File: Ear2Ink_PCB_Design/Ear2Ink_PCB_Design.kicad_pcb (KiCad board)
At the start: 2 copper layers, 68 parts, among them J1 Conn_02x16_Top_Bottom, J2 Conn_01x08_Pin, J3 Conn_01x08_Pin, J4 MEM2052-00-195-00-A_REVA, J5 Conn_01x06_Pin, J6 Conn_01x04_Pin, J7 Conn_01x03_Pin, P1 OSTTE020104, SW1 SW_Push, U1 STM32F411RETx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

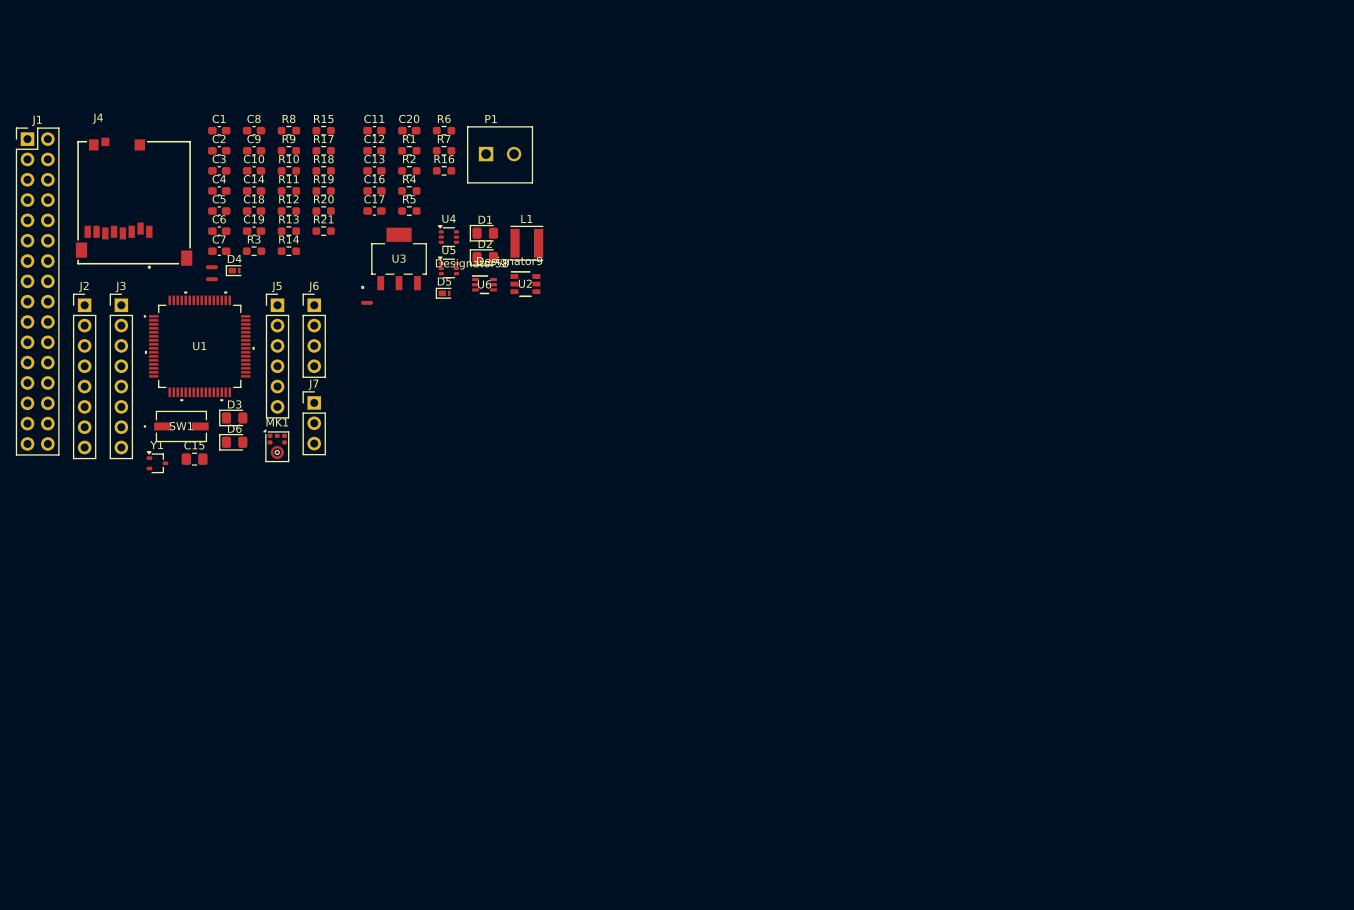
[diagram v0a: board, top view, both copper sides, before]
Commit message: components on board (no traces yet)
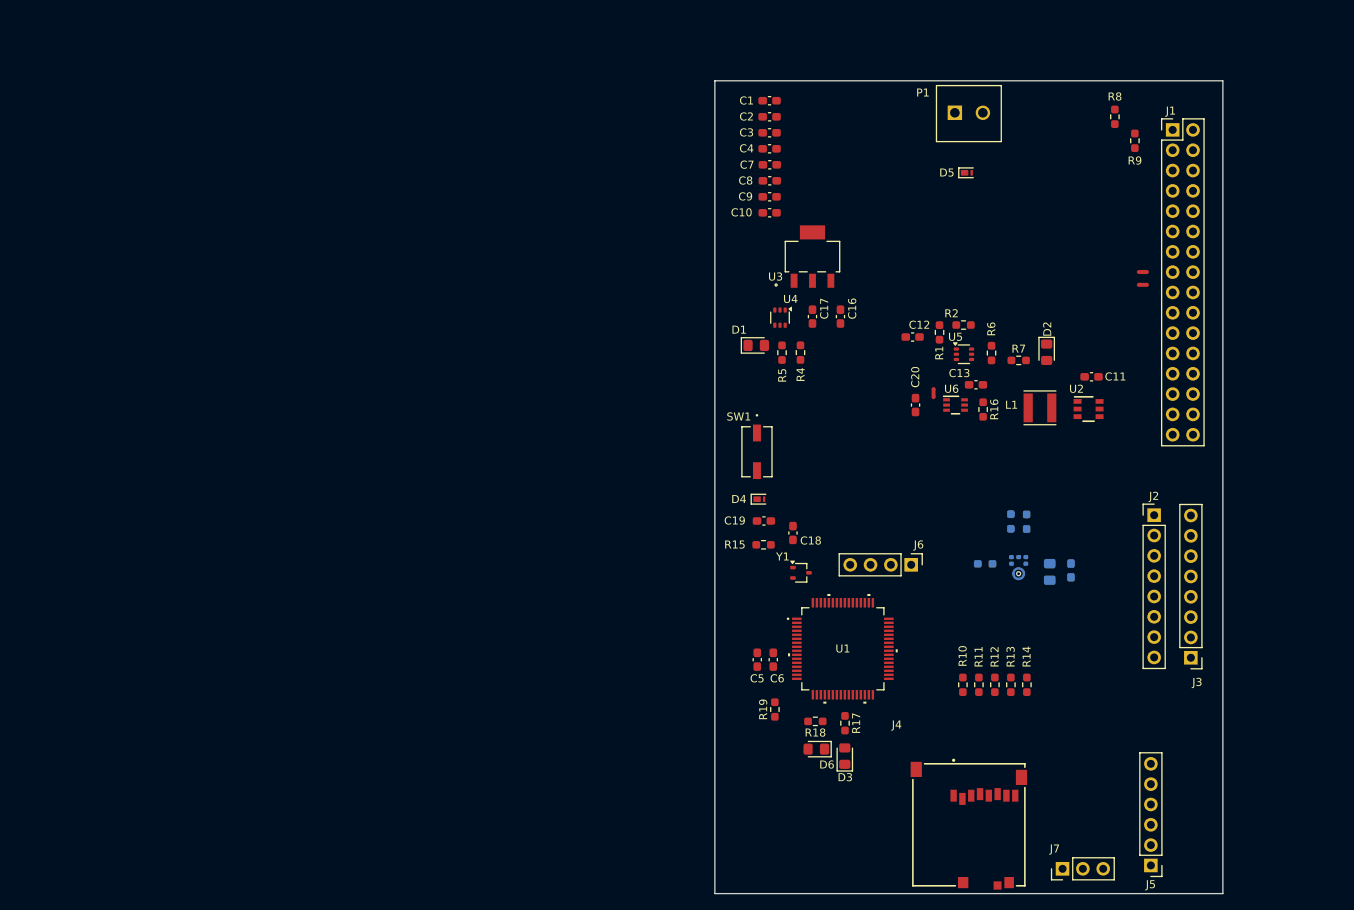
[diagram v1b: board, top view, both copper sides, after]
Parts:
- C14, C15, MK1, R20, R21, R3: moved to B.Cu
- moved J1 143.1 mm to (188.2, 37.1)
- moved J3 140.8 mm to (190.5, 103.1), turned to 180 degrees
- moved J2 136.2 mm to (185.9, 85.3)
- moved J4 130.1 mm to (162.8, 124.0), turned to 180 degrees
- moved J5 129.7 mm to (185.5, 129.1), turned to 180 degrees
- moved NT3 116.4 mm to (184.5, 56.5), turned to 180 degrees
- moved NT2 116.4 mm to (184.5, 54.9), turned to 180 degrees
- moved C14 112.6 mm to (175.5, 92.2), turned to -90 degrees
- moved J7 110.2 mm to (174.5, 129.5), turned to 90 degrees
- moved C15 107.8 mm to (172.9, 92.4), turned to -90 degrees
- moved R14 107.0 mm to (170.0, 106.5), turned to 90 degrees
- moved R13 106.6 mm to (168.0, 106.5), turned to 90 degrees
- moved R12 106.3 mm to (166.0, 106.5), turned to 90 degrees
- moved R11 106.1 mm to (164.0, 106.5), turned to 90 degrees
- moved R10 105.9 mm to (162.0, 106.5), turned to 90 degrees
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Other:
- board outline added: 63.5 x 101.6 mm

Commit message: some routing
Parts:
- moved J7 51.3 mm to (134.0, 98.0), turned to 180 degrees
- moved R14 10.0 mm to (160.0, 106.5), turned to -90 degrees
- moved Y1 5.04 mm to (145.0, 88.7)
- moved J6 3.88 mm to (158.0, 88.5)
- moved R12 2.19 mm to (168.0, 105.6), turned to 0 degrees
- moved D2 2.07 mm to (171.0, 63.5)
- moved D1 1.81 mm to (136.0, 65.9)
- moved R18 1.39 mm to (143.6, 112.5)
- moved R13 1.10 mm to (168.0, 107.6), turned to 0 degrees
- moved C19 1.00 mm to (137.1, 85.0)
- moved D4 1.00 mm to (136.6, 82.3)
- moved SW1 1.00 mm to (136.3, 76.4)
- moved R15 0.99 mm to (137.2, 88.0)
- moved C16 0.80 mm to (147.5, 60.5)
- moved R7 0.59 mm to (168.7, 65.4), turned to 90 degrees
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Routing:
- net +3.3V: track 0.00 -> 77.6 mm
- net SPI3_MISO: track 0.00 -> 31.7 mm
- net SPI3_MOSI: track 0.00 -> 31.7 mm
- net 5V: track 0.00 -> 24.2 mm
- net SPI3_SCK: track 0.00 -> 18.7 mm
- net SD_DAT1: track 0.00 -> 17.4 mm
- net SD_DAT2: track 0.00 -> 13.4 mm
- net CS: track 0.00 -> 13.3 mm
- net +3.3VA: track 0.00 -> 9.38 mm
- net NRST: track 0.00 -> 9.30 mm
- net 9V: track 0.00 -> 8.00 mm
- net Net-(U3-VO): track 0.00 -> 7.52 mm
- net Net-(U4-ST): track 0.00 -> 6.40 mm
- net Net-(U1-PC4): track 0.00 -> 5.88 mm
- net Net-(U5-VIN): track 0.00 -> 5.67 mm
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
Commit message: some pcb
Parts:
- removed C10: 4.7uF, Capacitor_SMD:C_0603_1608Metric_Pad1.08x0.95mm_HandSolder
- removed C7, C8: 0.1uF, Capacitor_SMD:C_0603_1608Metric_Pad1.08x0.95mm_HandSolder
- added C21: 4.7uF, Capacitor_SMD:C_0603_1608Metric_Pad1.08x0.95mm_HandSolder, F.Cu at (150.0, 74.0)
- moved R17 56.9 mm to (100.5, 79.4)
- moved D3 56.9 mm to (100.5, 83.5)
- moved D6 56.9 mm to (97.0, 82.5)
- moved R18 56.9 mm to (96.9, 80.0)
- moved R19 56.3 mm to (92.0, 77.6)
- moved C5 56.3 mm to (90.0, 71.4)
- moved C6 56.3 mm to (92.0, 71.4)
- moved J7 49.0 mm to (155.5, 54.0), turned to 90 degrees
- moved C20 41.9 mm to (176.4, 34.9)
- moved U6 41.9 mm to (181.4, 34.9)
- moved NT1 41.6 mm to (178.6, 33.7)
- moved C2 41.0 mm to (152.0, 74.0), turned to -90 degrees
- moved C1 40.2 mm to (145.2, 73.0), turned to -90 degrees
- moved R16 39.2 mm to (183.4, 37.8), turned to 180 degrees
- moved U1 38.8 mm to (148.0, 63.2)
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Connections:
- U1 pad 30: unconnected-(U1-VCAP1-Pad30) -> Net-(U1-VCAP1)
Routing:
- net SD_Detect: track 0.00 -> 54.9 mm
- net R4: track 4.62 -> 56.2 mm
- net R3: track 4.62 -> 55.6 mm
- net R2: track 4.62 -> 54.3 mm
- net R1: track 4.62 -> 53.2 mm
- net +3.3V: track 77.6 -> 32.2 mm
- net I2S2_WS: track 0.00 -> 36.6 mm, vias 0 -> 1
- net C1: track 4.62 -> 40.0 mm, vias 0 -> 1
- net SYS_SWCLK: track 0.00 -> 27.0 mm
- net Net-(U2-EN): track 0.00 -> 24.9 mm
- net Net-(U5-VIN): track 5.67 -> 29.8 mm
- net SPI3_MOSI: track 31.7 -> 8.46 mm
- net SPI3_MISO: track 31.7 -> 10.4 mm
- net NRST: track 9.30 -> 27.8 mm
- net 5V: track 24.2 -> 6.31 mm
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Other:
- board size 63.5 x 101.6 mm -> 63.5 x 69.8 mm

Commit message: more progress
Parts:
- removed R10, R11, R12, R13, R14: 10k, Resistor_SMD:R_0603_1608Metric_Pad0.98x0.95mm_HandSolder
- moved D6 55.6 mm to (152.0, 90.3)
- moved R18 55.6 mm to (151.9, 87.7)
- moved D3 49.0 mm to (149.0, 76.5)
- moved R17 48.9 mm to (149.0, 72.5)
- moved R19 48.2 mm to (139.5, 69.5), turned to 180 degrees
- moved C5 46.7 mm to (136.5, 67.6), turned to -90 degrees
- moved C6 42.7 mm to (134.5, 67.6), turned to -90 degrees
- moved NT2 7.90 mm to (185.8, 63.4)
- moved J7 7.08 mm to (162.4, 55.5)
- moved C18 3.21 mm to (137.8, 56.3), turned to 0 degrees
- moved C2 2.00 mm to (154.0, 74.0)
- moved C21 2.00 mm to (152.0, 74.0)
- moved R15 1.92 mm to (140.0, 72.6)
- moved C1 1.40 mm to (144.2, 74.0)
- moved C19 1.15 mm to (140.0, 77.0)
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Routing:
- net RS: track 0.00 -> 129.1 mm, vias 0 -> 3
- net R/W: track 0.00 -> 94.1 mm, vias 0 -> 4
- net ADC10: track 0.00 -> 92.6 mm, vias 0 -> 2
- net DB4: track 0.00 -> 80.6 mm, vias 0 -> 1
- net EN: track 0.00 -> 80.5 mm, vias 0 -> 2
- net DB6: track 0.00 -> 77.6 mm, vias 0 -> 2
- net DB5: track 0.00 -> 76.2 mm, vias 0 -> 1
- net SD_Detect: track 54.9 -> 0.00 mm
- net CS: track 0.00 -> 54.2 mm
- net SPI3_MISO: track 10.4 -> 61.5 mm
- net SPI3_SCK: track 12.6 -> 57.8 mm
- net SPI3_MOSI: track 8.46 -> 49.7 mm, vias 0 -> 1
- net +3.3V: track 32.2 -> 62.5 mm
- net SD_DAT2: track 0.08 -> 28.3 mm, vias 0 -> 1
- net 9V: track 8.68 -> 35.7 mm
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- added copper zone on F.Cu, net +3.3V
- added copper zone on B.Cu, net GND
- added copper zone on F.Cu, net GND

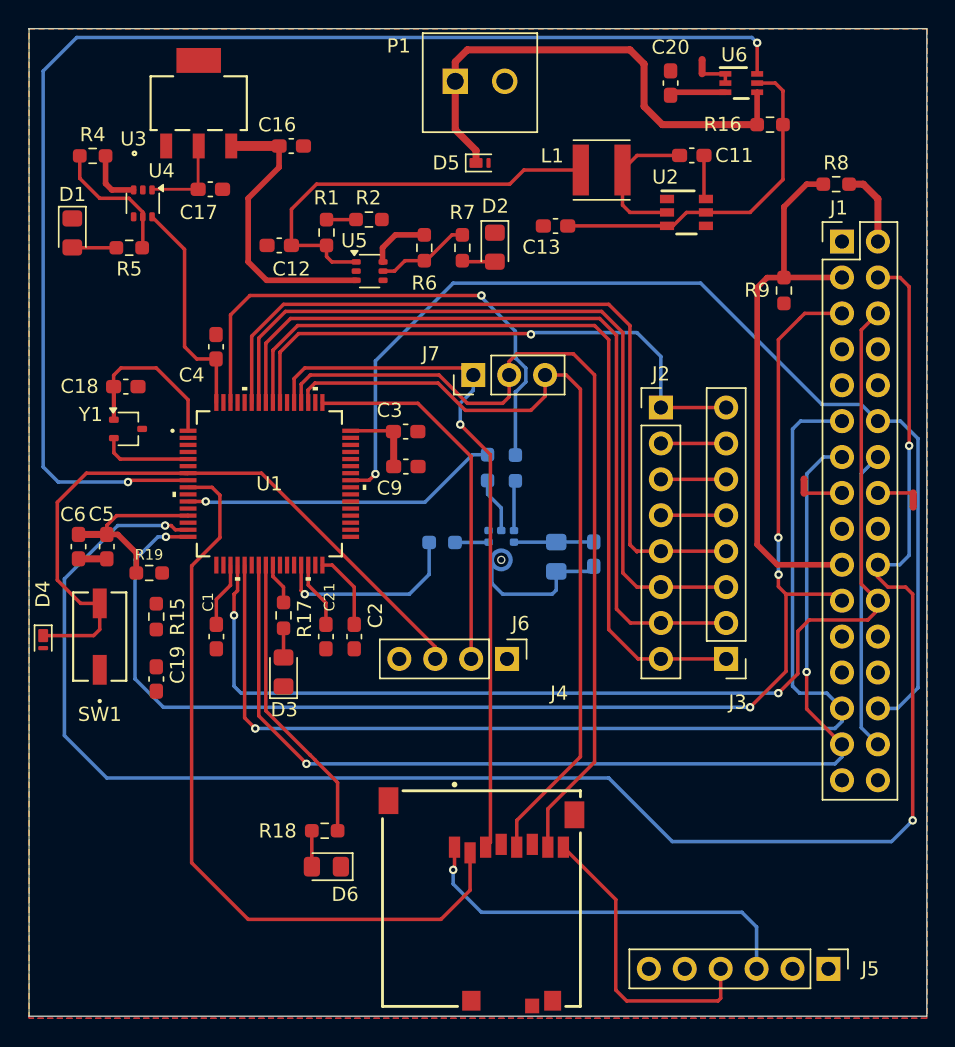
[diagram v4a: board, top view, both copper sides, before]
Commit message: ran DRC and fixed some errors
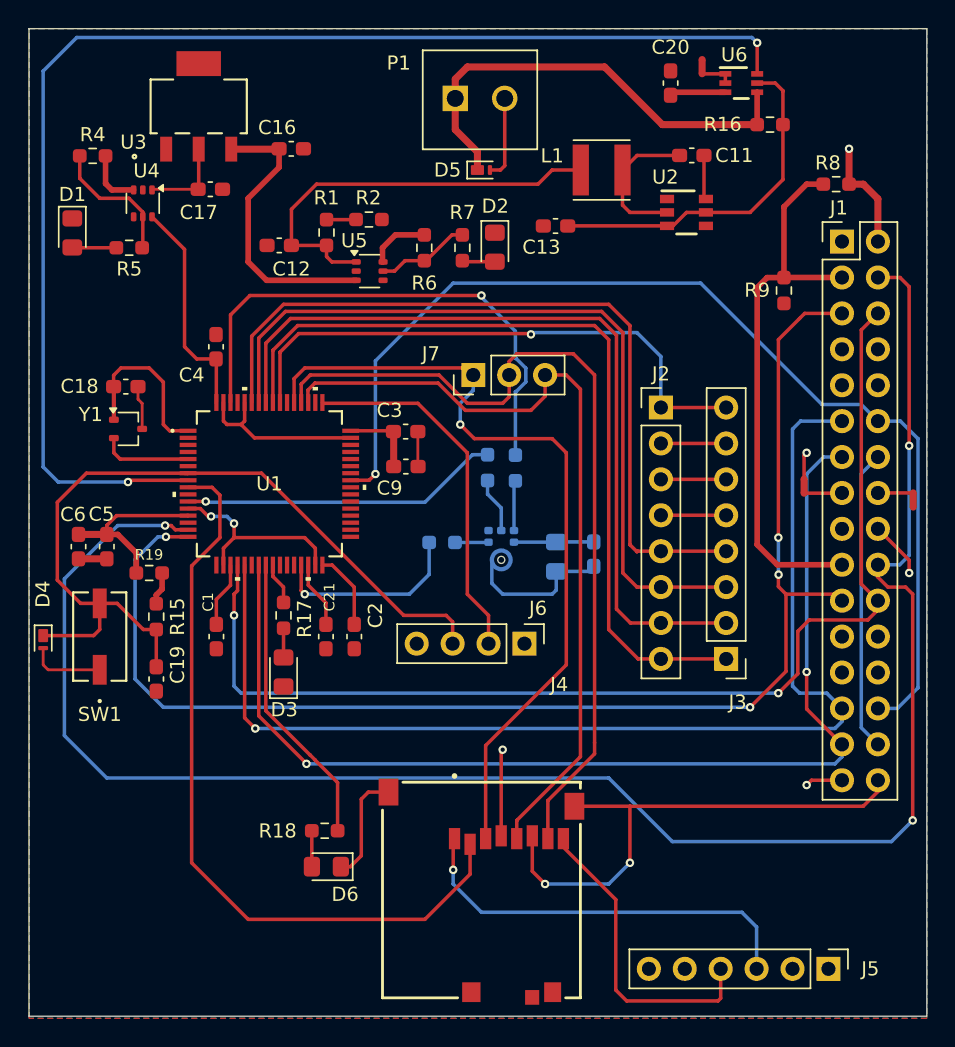
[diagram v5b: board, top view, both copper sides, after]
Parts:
- moved J6 1.64 mm to (166.0, 74.5)
- moved P1 1.21 mm to (162.9, 35.9)
- moved J4 0.61 mm to (163.0, 91.9)
- moved D5 0.51 mm to (163.0, 41.0)
- moved U3 0.23 mm to (143.0, 36.5)
- moved C16 0.20 mm to (149.5, 39.5)
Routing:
- net GND: track 12.8 -> 101.3 mm, vias 0 -> 4
- net +3.3V: track 62.5 -> 82.5 mm, vias 0 -> 5
- net NRST: track 49.1 -> 57.7 mm
- net SPI3_MOSI: track 49.7 -> 56.7 mm
- net 9V: track 35.7 -> 32.8 mm
- net SD_DAT2: track 28.3 -> 29.1 mm
- net SPI3_SCK: track 57.8 -> 57.2 mm
- net SPI3_MISO: track 61.5 -> 60.9 mm
- net SYS_SWCLK: track 26.4 -> 25.8 mm
- added copper zone on B.Cu, net +3.3V
- removed copper zone on F.Cu, net +3.3V
- removed copper zone on B.Cu, net GND

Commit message: fixed everything
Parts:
- added J8: Conn_01x16_Pin, Connector_PinHeader_2.54mm:PinHeader_1x16_P2.54mm_Vertical, F.Cu at (125.5, 84.2)
- added R10: 10k, Resistor_SMD:R_0603_1608Metric_Pad0.98x0.95mm_HandSolder, F.Cu at (153.8, 88.8)
- added R11: 10k, Resistor_SMD:R_0603_1608Metric_Pad0.98x0.95mm_HandSolder, F.Cu at (151.3, 96.3)
- added R12: 10k, Resistor_SMD:R_0603_1608Metric_Pad0.98x0.95mm_HandSolder, F.Cu at (179.4, 91.0)
- added R13: 10k, Resistor_SMD:R_0603_1608Metric_Pad0.98x0.95mm_HandSolder, F.Cu at (153.5, 96.4)
- added R14: 10k, Resistor_SMD:R_0603_1608Metric_Pad0.98x0.95mm_HandSolder, F.Cu at (179.5, 93.1)
- J1: value Conn_02x16_Top_Bottom -> Conn_01x16_Pin; footprint Connector_PinHeader_2.54mm:PinHeader_2x16_P2.54mm_Vertical -> Connector_PinHeader_2.54mm:PinHeader_1x16_P2.54mm_Vertical
- moved J1 70.2 mm to (129.6, 84.2), turned to 180 degrees
- moved NT3 68.5 mm to (127.5, 46.0), turned to 0 degrees
- moved R8 65.6 mm to (134.7, 80.0), turned to 90 degrees
- moved NT2 60.1 mm to (127.6, 48.6), turned to 0 degrees
- moved R9 56.8 mm to (136.5, 80.0)
- moved C11 31.6 mm to (146.9, 33.8)
- moved U2 31.6 mm to (146.6, 37.8)
- moved L1 31.3 mm to (140.5, 36.4), turned to -90 degrees
- moved C14 28.2 mm to (173.8, 40.2), turned to 0 degrees
- moved R16 27.5 mm to (156.1, 34.9), turned to 0 degrees
- moved D1 27.4 mm to (161.4, 43.9), turned to 90 degrees
- moved D2 26.9 mm to (137.1, 47.3), turned to 0 degrees
- moved C15 26.9 mm to (174.1, 42.1), turned to 0 degrees
- moved U6 25.6 mm to (156.0, 38.3), turned to 90 degrees
- moved NT1 25.1 mm to (154.2, 39.9), turned to -90 degrees
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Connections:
- J1 pad 15: LED+ -> +3.3V
- J1 pad 16: LED- -> GND
- J5 pad 3: SD_DAT2 -> SD_DAT1
- J5 pad 4: SD_DAT1 -> SD_DAT2
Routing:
- net +3.3V: track 82.5 -> 282.5 mm, vias 5 -> 22
- net RS: track 129.1 -> 24.8 mm, vias 3 -> 2
- net R/W: track 94.1 -> 25.2 mm, vias 4 -> 2
- net ADC10: track 92.6 -> 35.0 mm
- net SDIO_CK: track 0.00 -> 56.9 mm, vias 0 -> 2
- net SDIO_D0: track 0.00 -> 56.0 mm, vias 0 -> 2
- net SDIO_CMD: track 0.00 -> 53.2 mm, vias 0 -> 2
- net C4: track 4.62 -> 54.8 mm, vias 0 -> 2
- net C3: track 4.62 -> 53.4 mm, vias 0 -> 2
- net C2: track 4.62 -> 53.3 mm, vias 0 -> 2
- net DB6: track 77.6 -> 32.6 mm
- net DB5: track 76.2 -> 36.3 mm
- net SD_Detect: track 0.00 -> 37.6 mm
- net I2S2_CK: track 13.8 -> 45.0 mm
- net Vee: track 39.5 -> 11.0 mm
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- added copper zone on F.Cu, net +3.3V
- added copper zone on F.Cu, net 5V
- added copper zone on F.Cu, net 9V
- added copper zone on B.Cu, net GND
